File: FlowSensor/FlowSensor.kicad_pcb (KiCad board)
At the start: 2 copper layers, 12 parts, among them P1 CONN_01X08, P2 CONN_01X08, U1 LMC6062, U2 TLV493D-A1B6

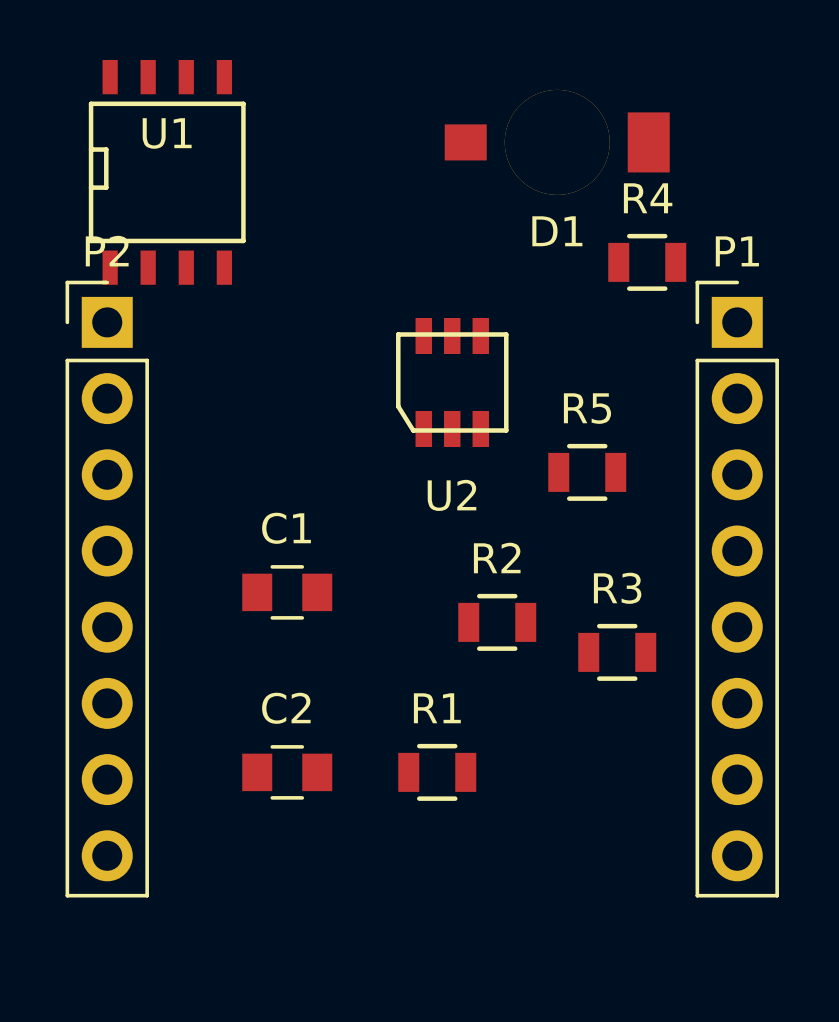
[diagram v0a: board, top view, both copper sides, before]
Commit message: Got the bug fixed with the layout.
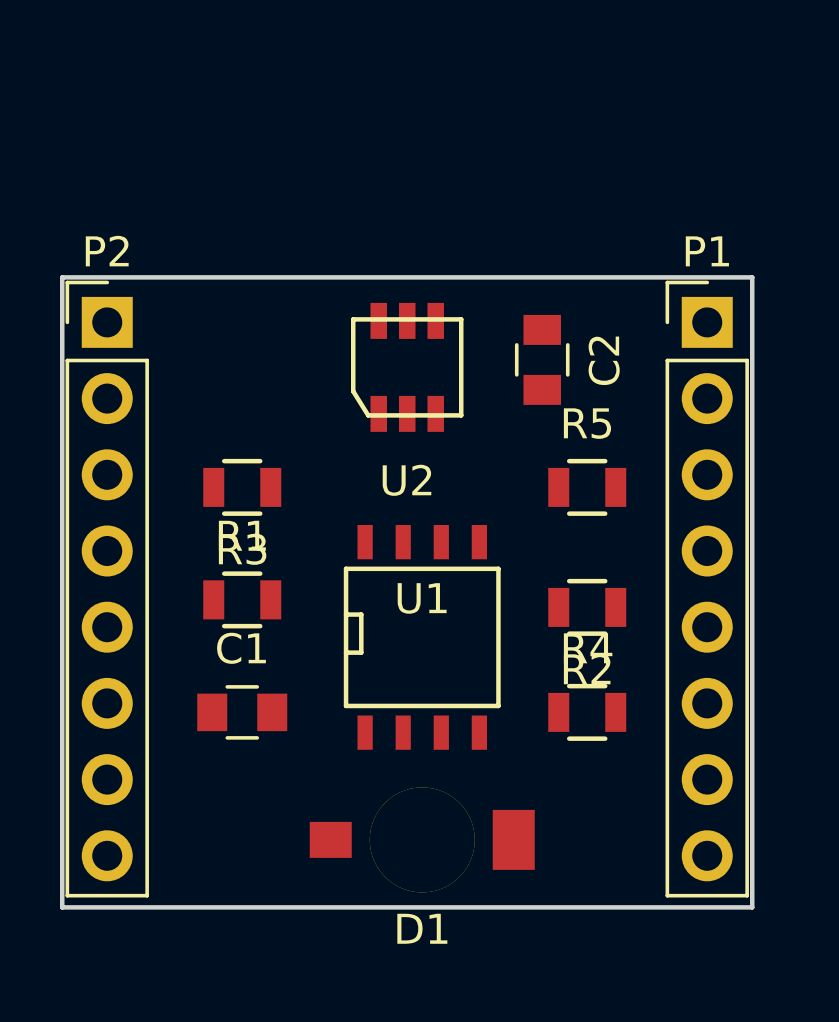
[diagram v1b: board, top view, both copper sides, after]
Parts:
- moved D1 23.7 mm to (147.5, 120.2)
- moved U1 17.7 mm to (147.5, 113.5)
- moved C2 16.2 mm to (151.5, 104.2), turned to 270 degrees
- moved R4 15.1 mm to (153.0, 116.0)
- moved R3 13.7 mm to (141.5, 108.5), turned to 180 degrees
- moved R1 8.68 mm to (141.5, 112.2)
- moved C1 4.27 mm to (141.5, 116.0)
- moved R2 3.04 mm to (153.0, 112.5), turned to 180 degrees
- moved U2 1.58 mm to (147.0, 104.5)
- moved P1 1.00 mm to (157.0, 103.0)
- moved R5 0.50 mm to (153.0, 108.5)
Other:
- board outline added: 23 x 21 mm

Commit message: Finished layout of SensorNode and FlowMeter boards.
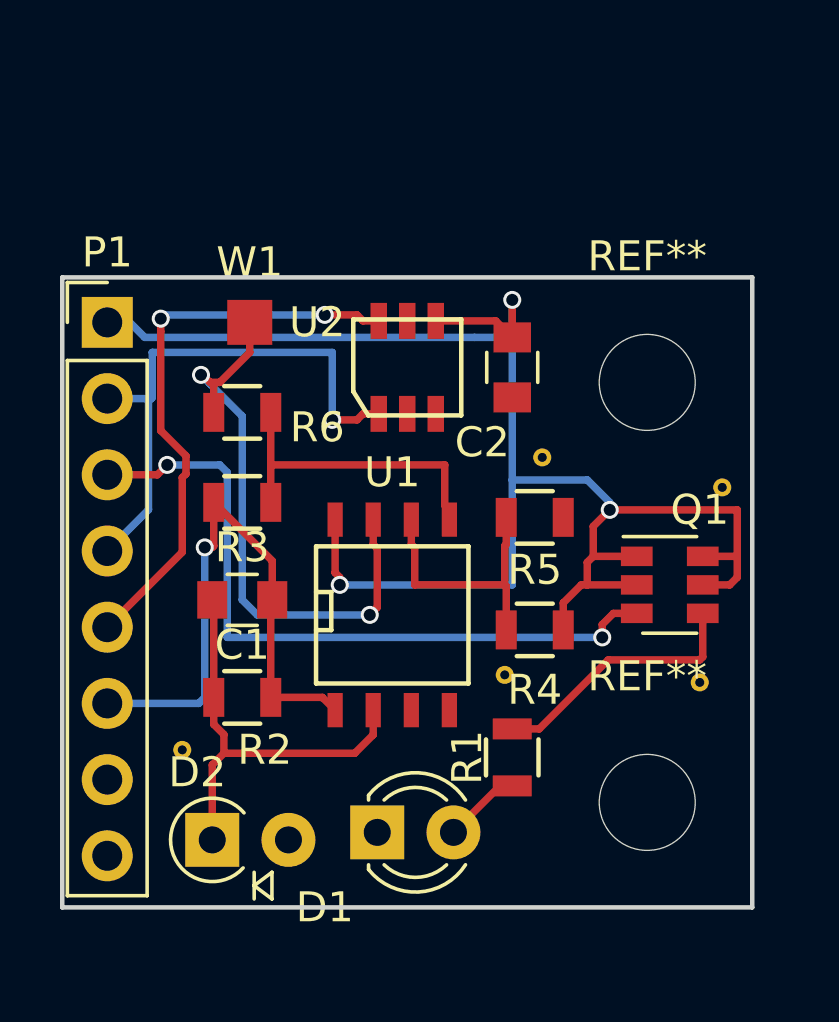
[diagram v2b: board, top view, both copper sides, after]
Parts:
- removed P2: CONN_01X08, Socket_Strips:Socket_Strip_Straight_1x08_Pitch2.54mm
- added D2: PD15-21B/TR8, Diodes_ThroughHole:D_A-405_P2.54mm_Vertical_AnodeUp, F.Cu at (140.5, 120.2)
- added Q1: FDC606P, TO_SOT_Packages_SMD:SOT-23-6, F.Cu at (155.8, 111.8)
- added R6: 100K, Resistors_SMD:R_0805, F.Cu at (141.5, 106.0)
- added REF**: via_0.3mm, KicadFootprint:via_0.3mm, F.Cu at (151.5, 107.5)
- added REF**: via_0.3mm, KicadFootprint:via_0.3mm, F.Cu at (157.5, 108.5)
- added REF**: via_0.3mm, KicadFootprint:via_0.3mm, F.Cu at (156.8, 115.0)
- added REF**: via_0.3mm, KicadFootprint:via_0.3mm, F.Cu at (150.2, 114.8)
- added REF**: MountingHole_3.2mm_M3, Mounting_Holes:MountingHole_3.2mm_M3, F.Cu at (155.0, 119.0)
- added REF**: MountingHole_3.2mm_M3, Mounting_Holes:MountingHole_3.2mm_M3, F.Cu at (155.0, 105.0)
- added REF**: via_0.3mm, KicadFootprint:via_0.3mm, F.Cu at (139.5, 117.2)
- added W1: TEST_1P, Measurement_Points:Measurement_Point_Square-SMD-Pad_Small, F.Cu at (141.8, 103.0)
- D1: value PD15-21B/TR8 -> LED; footprint KicadFootprint:2-SMD_Z-Bend -> LEDs:LED_D3.0mm_FlatTop
- R1: value 1M -> 100
- R2: value 6K -> 1M
- R3: value 100k -> 6K
- R5: value 100K -> 100k
- moved P1 20.0 mm to (137.0, 103.0)
- moved R2 11.9 mm to (141.5, 115.5)
- moved R1 10.4 mm to (150.5, 117.5), turned to 270 degrees
- moved C1 3.75 mm to (141.5, 112.2), turned to 180 degrees
- moved R4 3.26 mm to (151.2, 113.2)
- moved R5 2.02 mm to (151.2, 109.5), turned to 180 degrees
- moved D1 1.52 mm to (146.0, 120.0)
- moved U1 1.25 mm to (146.5, 112.8)
- moved C2 1.03 mm to (150.5, 104.5)
- moved R3 0.50 mm to (141.5, 109.0)
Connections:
- D1 pad 1: Net-(C1-Pad2) -> GND
- D1 pad 2: GND -> Net-(D1-Pad2)
- P1 pad 1: (no net) -> VDD
- P1 pad 2: (no net) -> /GPIO1
- P1 pad 3: (no net) -> /GPIO2
- P1 pad 4: (no net) -> /GPIO1
- P1 pad 5: (no net) -> /SDA
- P1 pad 6: (no net) -> /ANALOG1
- R1 pad 1: /ANALOG1 -> Net-(Q1-Pad4)
- R1 pad 2: Net-(C1-Pad2) -> Net-(D1-Pad2)
- R2 pad 1: Net-(R2-Pad1) -> /ANALOG1
- R2 pad 2: /ANALOG1 -> Net-(C1-Pad2)
- R3 pad 2: VDD -> /ANALOG1
- R4 pad 1: GND -> Net-(R4-Pad1)
- R4 pad 2: Net-(R3-Pad1) -> VDD
- R5 pad 1: /ANALOG2 -> GND
- R5 pad 2: Net-(R2-Pad1) -> Net-(R4-Pad1)
- U1 pad 5: Net-(R2-Pad1) -> Net-(R3-Pad1)
- U1 pad 6: Net-(R3-Pad1) -> Net-(R4-Pad1)
- U1 pad 7: /ANALOG2 -> Net-(R6-Pad1)
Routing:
- net VDD: track 0.00 -> 55.8 mm, vias 0 -> 3
- net /GPIO2: track 0.00 -> 24.0 mm, vias 0 -> 2
- net Net-(R6-Pad1): track 0.00 -> 20.1 mm, vias 0 -> 2
- net /ANALOG1: track 0.00 -> 19.8 mm, vias 0 -> 1
- net /SDA: track 0.00 -> 19.1 mm, vias 0 -> 2
- net /GPIO1: track 0.00 -> 18.6 mm, vias 0 -> 1
- net Net-(C1-Pad2): track 0.00 -> 14.4 mm
- net Net-(R3-Pad1): track 0.00 -> 10.7 mm
- net Net-(R4-Pad1): track 0.00 -> 9.01 mm
- net Net-(Q1-Pad4): track 0.00 -> 8.79 mm
- net Net-(D1-Pad2): track 0.00 -> 2.60 mm
- added copper zone on B.Cu, net GND
- added copper zone on F.Cu, net GND
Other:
- board text added: "FlowSensor Rev A"
